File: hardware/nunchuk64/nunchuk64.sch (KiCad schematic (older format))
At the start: 26 parts, among them J1 DB9_Female, J2 DB9_Female, J3 Conn_02x03_Odd_Even, P1 CONN_WII, P2 CONN_WII, Q1 BSS138, Q2 BSS138, Q3 BSS138, Q4 BSS138, SW1 SW_Push, U1 AMS1117-3V3, U2 ATMEGA328P-AU

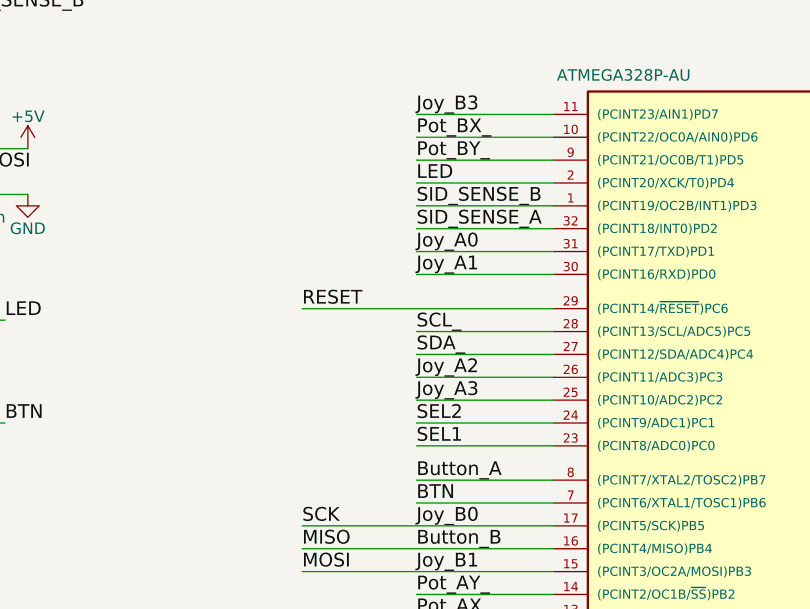
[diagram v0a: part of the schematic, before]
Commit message: added cosmetic change in layout
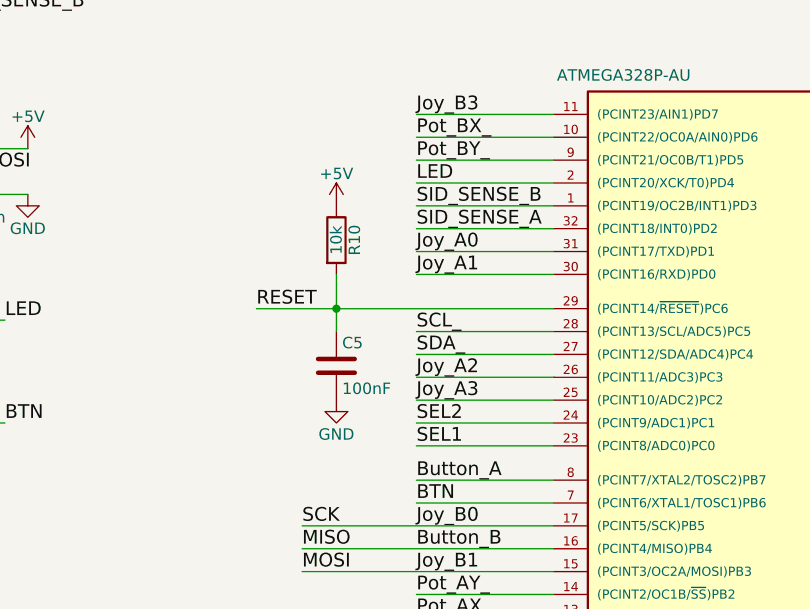
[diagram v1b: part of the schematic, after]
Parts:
- added C5: 100nF, Capacitors_SMD:C_0805_HandSoldering, symbol C
- added R10: 10k, Resistors_SMD:R_0805_HandSoldering, symbol R
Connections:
- net +5V: now also R10.1
- net GND: now also C5.2
- net RESET: now also C5.1, R10.2
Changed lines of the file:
@@
 LIBS:contrib
 LIBS:valves
+LIBS:nunchuk64-cache
 EELAYER 25 0
 EELAYER END
@@
 Text Label 6600 4950 0    60   ~ 0
 MISO
-Text Label 6600 3900 0    60   ~ 0
+Text Label 6400 3900 0    60   ~ 0
 RESET
 Text Label 6600 4850 0    60   ~ 0
 SCK
 Wire Wire Line
-	6600 3900 7700 3900
+	6400 3900 7700 3900
 $Comp
 L CP1 C1
@@
 Wire Wire Line
 	7100 4750 7700 4750
+$Comp
+L R R10
+U 1 1 5A96FB59
+P 6750 3600
+F 0 "R10" V 6830 3600 50  0000 C CNN
+F 1 "10k" V 6750 3600 50  0000 C CNN
+F 2 "Resistors_SMD:R_0805_HandSoldering" V 6680 3600 50  0001 C CNN
+F 3 "" H 6750 3600 50  0001 C CNN
+	1    6750 3600
+	1    0    0    -1
+$EndComp
+$Comp
+L C C5
+U 1 1 5A96FBD6
+P 6750 4150
+F 0 "C5" H 6775 4250 50  0000 L CNN
+F 1 "100nF" H 6775 4050 50  0000 L CNN
+F 2 "Capacitors_SMD:C_0805_HandSoldering" H 6788 4000 50  0001 C CNN
+F 3 "" H 6750 4150 50  0001 C CNN
+	1    6750 4150
+	1    0    0    -1
+$EndComp
+$Comp
+L +5V #PWR029
+U 1 1 5A96FC8D
+P 6750 3450
+F 0 "#PWR029" H 6750 3300 50  0001 C CNN
+F 1 "+5V" H 6750 3590 50  0000 C CNN
+F 2 "" H 6750 3450 50  0001 C CNN
+F 3 "" H 6750 3450 50  0001 C CNN
+	1    6750 3450
+	1    0    0    -1
+$EndComp
+$Comp
+L GND #PWR030
+U 1 1 5A96FCEC
+P 6750 4300
+F 0 "#PWR030" H 6750 4050 50  0001 C CNN
+F 1 "GND" H 6750 4150 50  0000 C CNN
+F 2 "" H 6750 4300 50  0001 C CNN
+F 3 "" H 6750 4300 50  0001 C CNN
+	1    6750 4300
+	1    0    0    -1
+$EndComp
+Wire Wire Line
+	6750 3750 6750 4000
+Connection ~ 6750 3900
 $EndSCHEMATC

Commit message: added cases/README.md
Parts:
- C1, C2: symbol CP1 -> nunchuk64-rescue:CP1
- C3, C4, C5: symbol C -> nunchuk64-rescue:C
- D1: symbol LED -> nunchuk64-rescue:LED
- J1, J2: symbol DB9_Female -> nunchuk64-rescue:DB9_Female
- J3: symbol Conn_02x03_Odd_Even -> nunchuk64-rescue:Conn_02x03_Odd_Even
- P1, P2: symbol CONN_WII -> conn_wii:CONN_WII
- Q1, Q2, Q3, Q4: symbol BSS138 -> nunchuk64-rescue:BSS138
- R1, R10, R2, R3, R4, R5, R6, R7, R8, R9: symbol R -> nunchuk64-rescue:R
- SW1: symbol SW_Push -> nunchuk64-rescue:SW_Push
- U1: symbol AMS1117-3V3 -> AMS1117-3V3:AMS1117-3V3
- U2: symbol ATMEGA328P-AU -> nunchuk64-rescue:ATMEGA328P-AU
